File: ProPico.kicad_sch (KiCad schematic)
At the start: 55 parts, among them J1 USB_C_Receptacle_USB2.0, J2 SWD, J3 LEFT, J4 RIGHT, SW1 BOOTSEL, SW2 RES, U1 FM24CL16B, U2 W25Q16JVUXIQ, U3 AMS1117-3.3, U4 LM4040DBZ-3, U5 RP2040, Y1 ECS-120-12-36-AGN-TR3

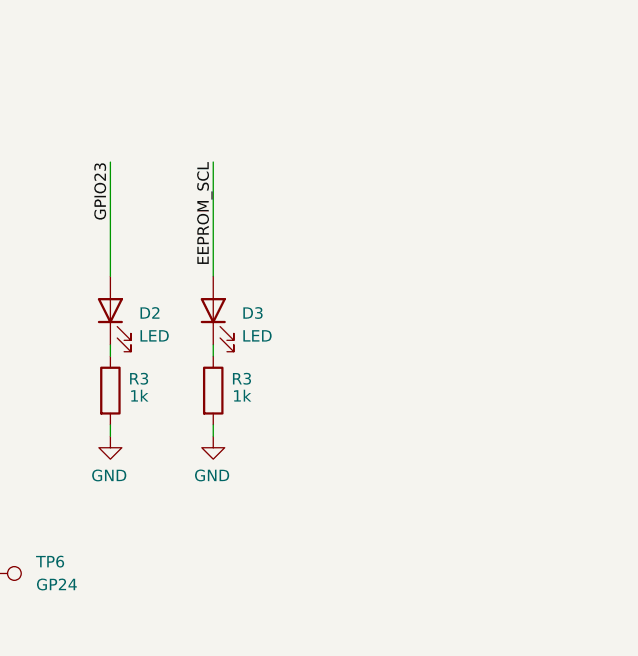
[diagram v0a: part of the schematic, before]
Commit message: added critical feature; neopixel
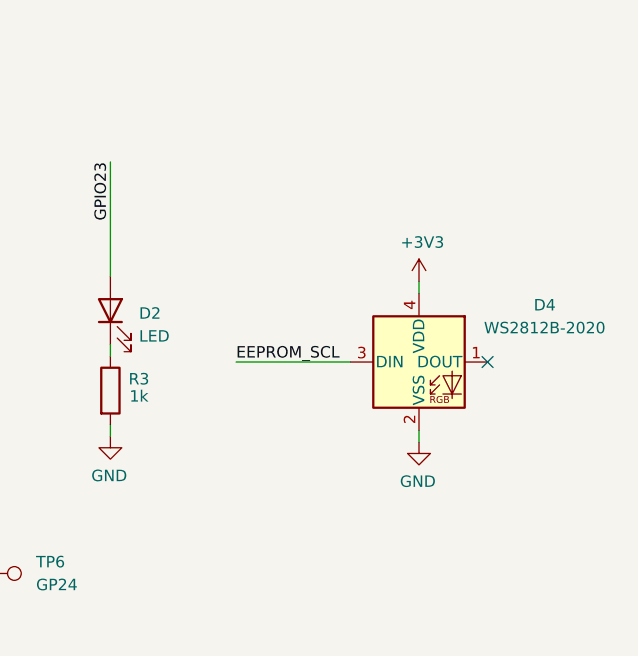
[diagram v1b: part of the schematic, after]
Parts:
- removed D3: LED, LED_SMD:LED_0603_1608Metric_Pad1.05x0.95mm_HandSolder, symbol Device:LED
- removed R3: 1k, Resistor_SMD:R_0402_1005Metric, symbol Device:R
- added D4: WS2812B-2020, LED_SMD:LED_WS2812B-2020_PLCC4_2.0x2.0mm, symbol LED:WS2812B-2020
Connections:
- net +3V3: now also D4.4 (VDD)
- net EEPROM_SCL: now also D4.3 (DIN)
- net GND: now also D4.2 (VSS)
- no-connect marks 2 -> 3
